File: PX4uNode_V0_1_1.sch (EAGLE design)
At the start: 133 parts, among them M3_MOUNT1101 MOUNT-HOLE3.1MM, M3_MOUNT1102 MOUNT-HOLE3.1MM, M3_MOUNT1103 MOUNT-HOLE3.1MM, M3_MOUNT1104 MOUNT-HOLE3.1MM, U101 STM32F4X7VX, U401 MAX3051, U402 MAX3051, X101 3.2x2.5 mm / 24 MHz / 15 ppm

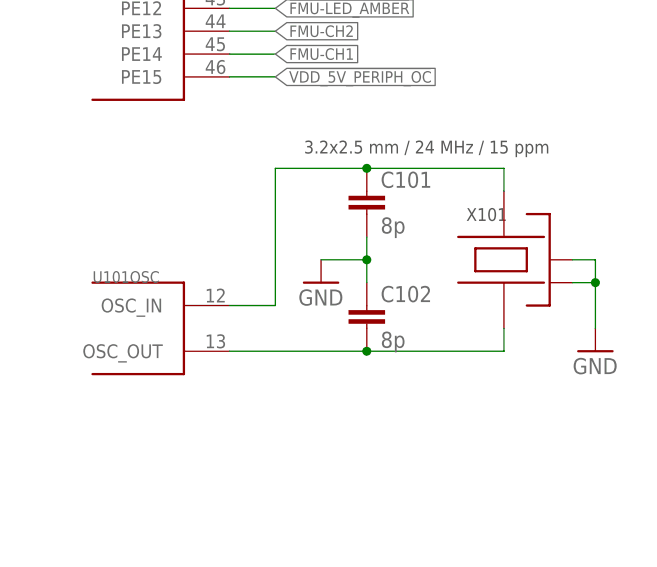
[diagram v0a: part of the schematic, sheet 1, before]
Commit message: A little more grounding
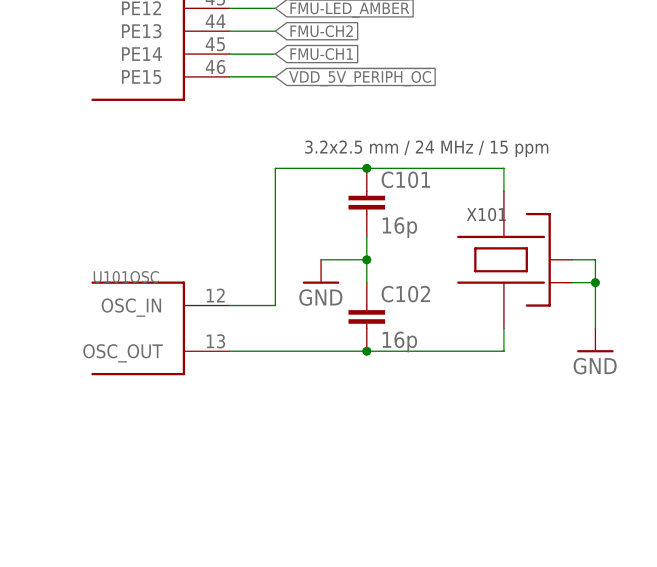
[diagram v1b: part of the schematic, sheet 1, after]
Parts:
- C101, C102: value 8p -> 16p; PARTNO C1005C0G1H080C -> C1005C0G1H160
- X101: PARTNO NX3225SA-24.000000MHZ -> ABM8G-24.000MHZ-4Y-T3
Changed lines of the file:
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@@
 <parts>
 <part name="X101" library="pixhawk2" deviceset="OSCILLATOR" device="-3.2X2.5" value="3.2x2.5 mm / 24 MHz / 15 ppm">
-<attribute name="PARTNO" value="NX3225SA-24.000000MHZ"/>
+<attribute name="PARTNO" value="ABM8G-24.000MHZ-4Y-T3"/>
 </part>
-<part name="C101" library="pixhawk2" deviceset="CAP" device="0402" value="8p">
-<attribute name="PARTNO" value="C1005C0G1H080C"/>
+<part name="C101" library="pixhawk2" deviceset="CAP" device="0402" value="16p">
+<attribute name="PARTNO" value="C1005C0G1H160"/>
 </part>
-<part name="C102" library="pixhawk2" deviceset="CAP" device="0402" value="8p">
-<attribute name="PARTNO" value="C1005C0G1H080C"/>
+<part name="C102" library="pixhawk2" deviceset="CAP" device="0402" value="16p">
+<attribute name="PARTNO" value="C1005C0G1H160"/>
 </part>
 <part name="GND1" library="SparkFun" deviceset="GND" device=""/>

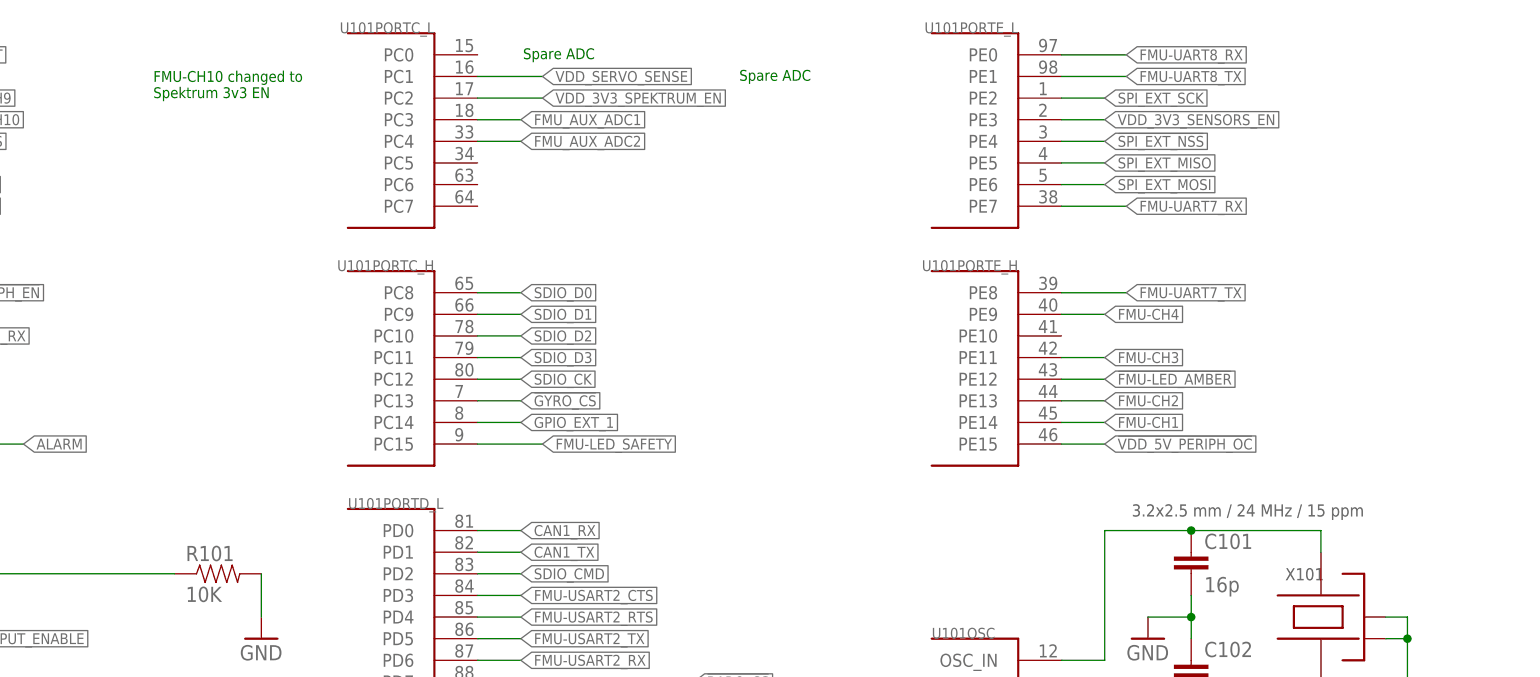
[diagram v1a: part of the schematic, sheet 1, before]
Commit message: General track thickening
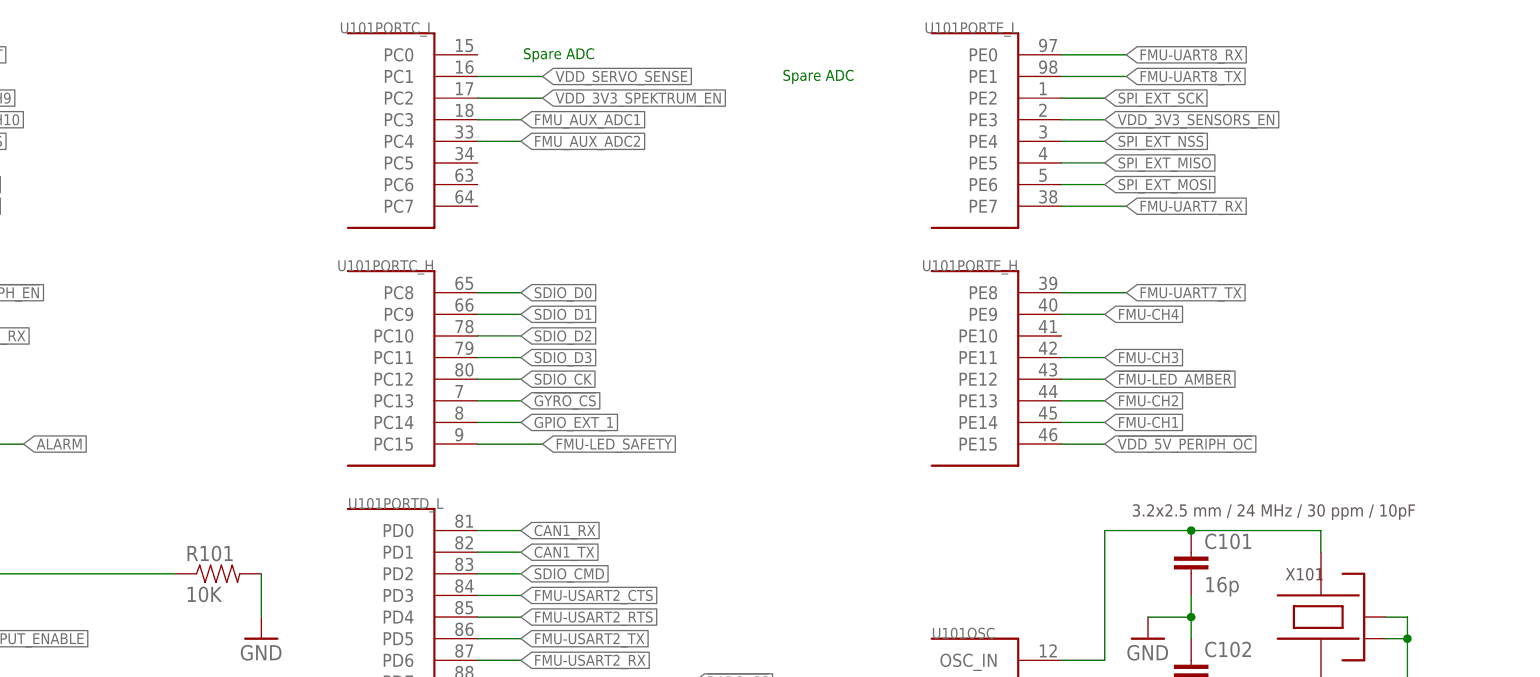
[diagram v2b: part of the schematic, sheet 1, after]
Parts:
- X101: value 3.2x2.5 mm / 24 MHz / 15 ppm -> 3.2x2.5 mm / 24 MHz / 30 ppm / 10pF
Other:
- note removed: "FMU-CH10 changed to Spektrum 3v3 EN"
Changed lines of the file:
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@@
 </classes>
 <parts>
-<part name="X101" library="pixhawk2" deviceset="OSCILLATOR" device="-3.2X2.5" value="3.2x2.5 mm / 24 MHz / 15 ppm">
+<part name="X101" library="pixhawk2" deviceset="OSCILLATOR" device="-3.2X2.5" value="3.2x2.5 mm / 24 MHz / 30 ppm / 10pF">
 <attribute name="PARTNO" value="ABM8G-24.000MHZ-4Y-T3"/>
 </part>
@@
 <text x="131.826" y="62.992" size="1.27" layer="91">Spare PWM output</text>
 <text x="112.014" y="164.592" size="1.27" layer="91">Spare ADC</text>
-<text x="137.414" y="162.052" size="1.27" layer="91">Spare ADC</text>
-<text x="68.58" y="160.02" size="1.27" layer="91">FMU-CH10 changed to
-Spektrum 3v3 EN</text>
+<text x="142.494" y="162.052" size="1.27" layer="91">Spare ADC</text>
 </plain>
 <instances>

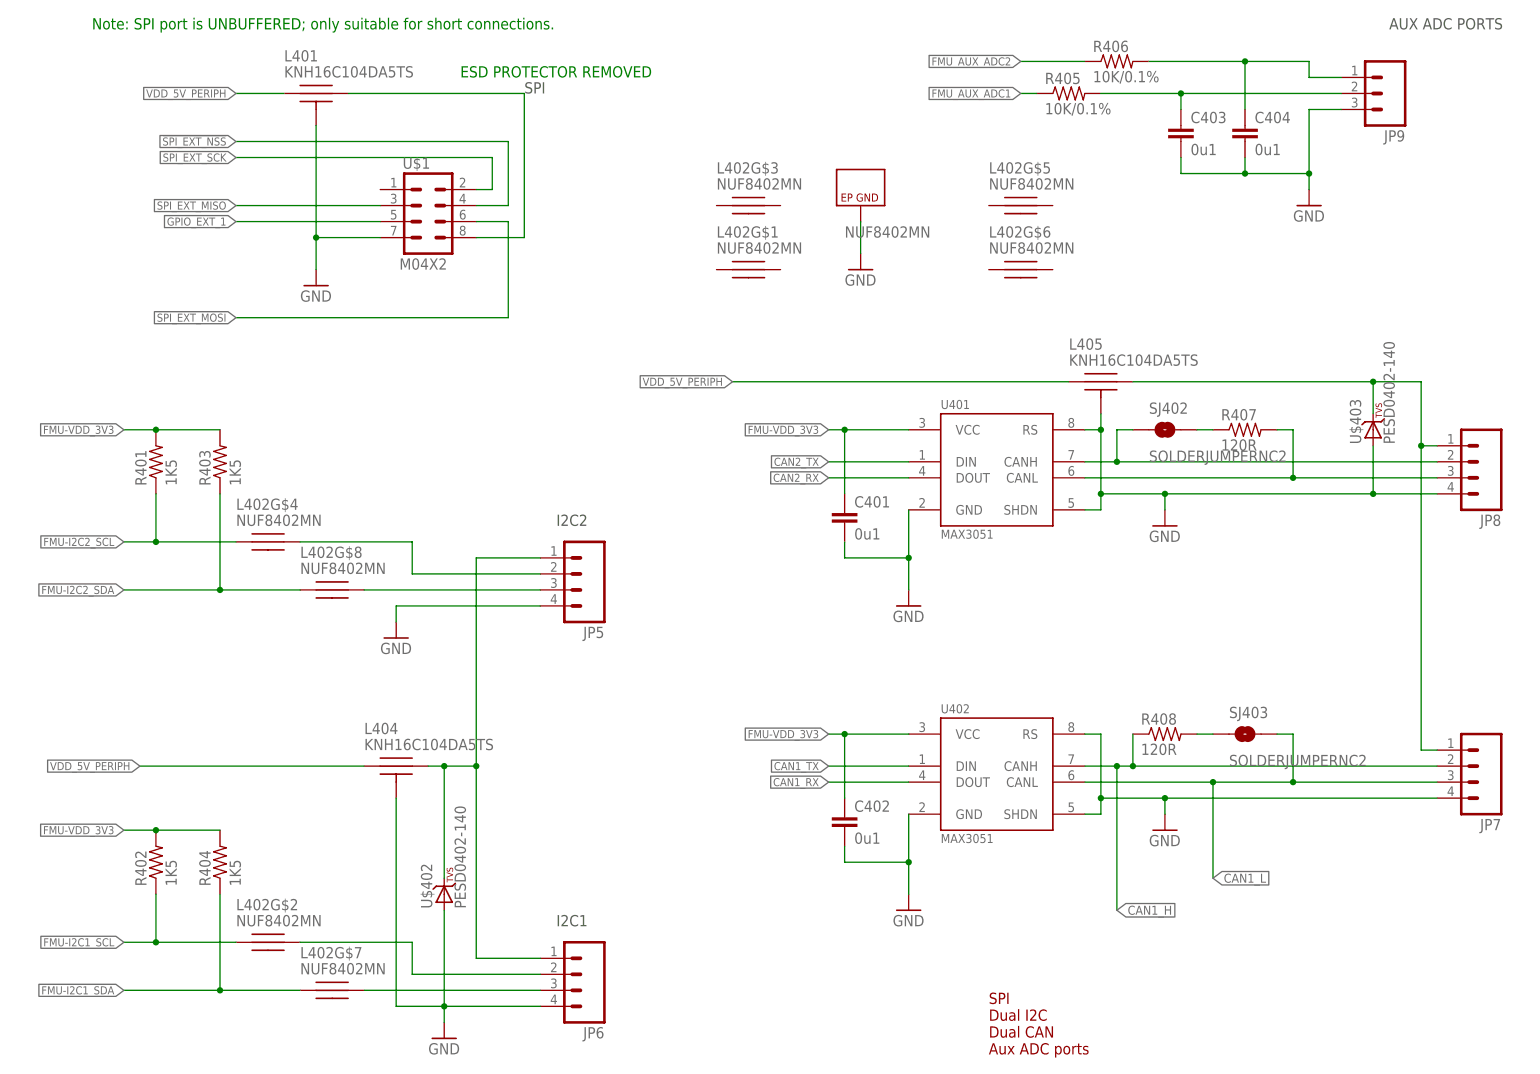
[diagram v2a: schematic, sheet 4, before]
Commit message: Added PARTNO and EXCLUDE to BOM. Parts renumbered
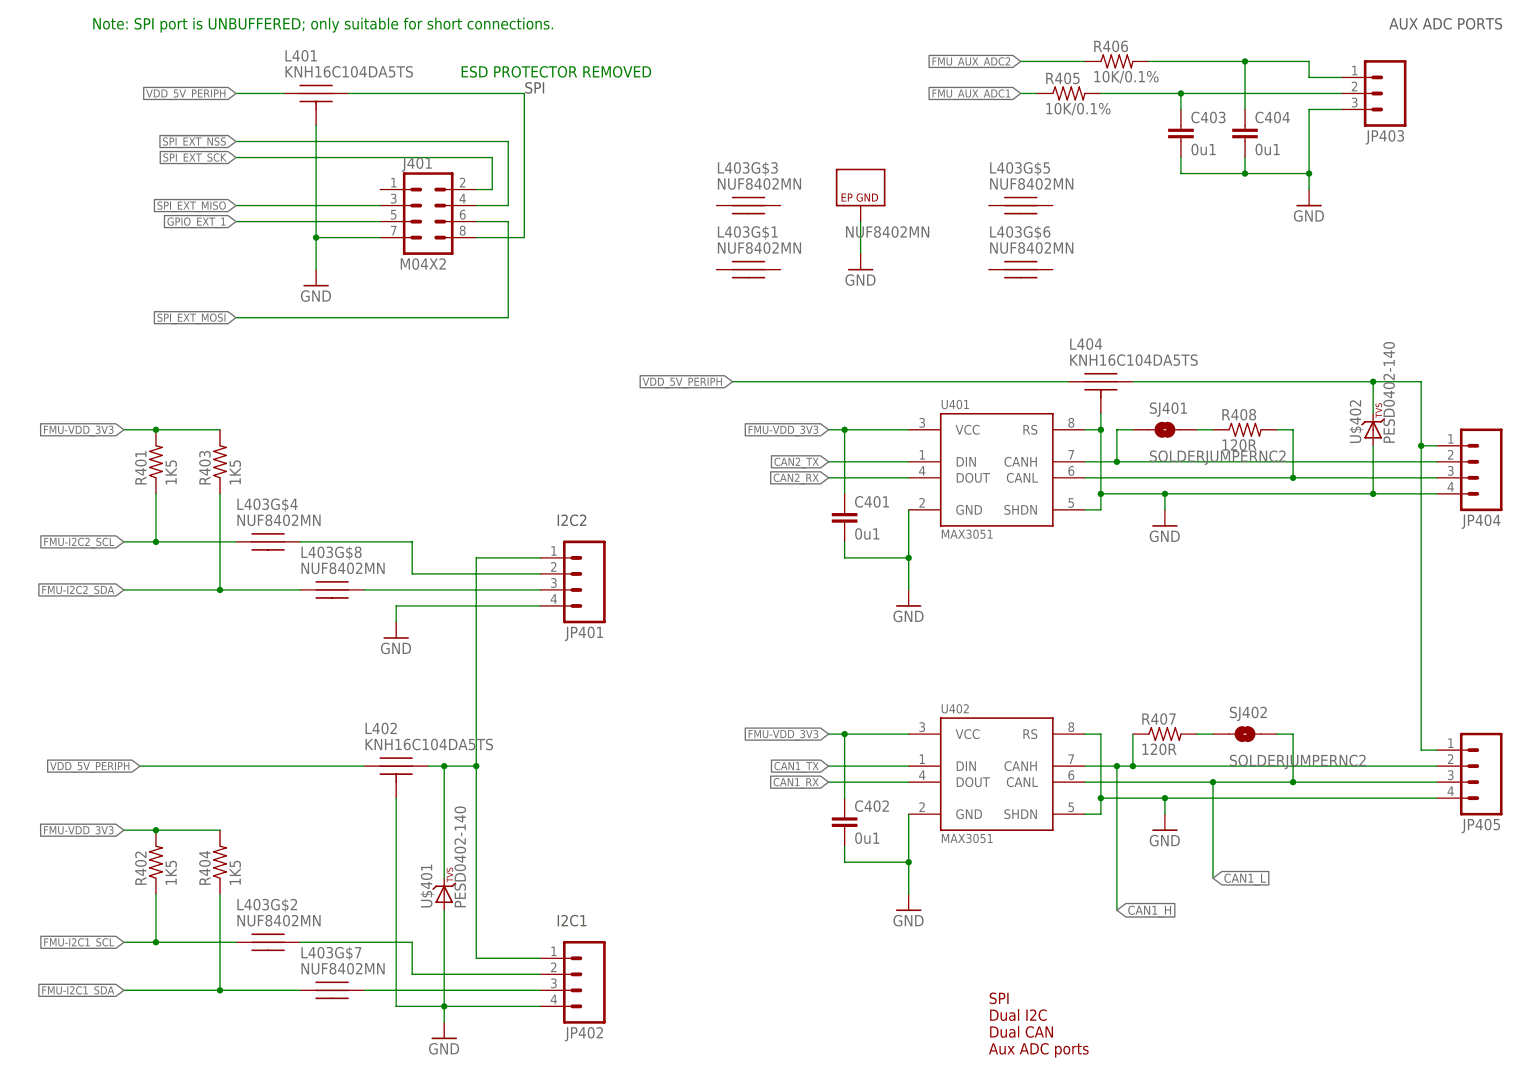
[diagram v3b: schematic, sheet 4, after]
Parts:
- removed C607: 22uF, SparkFun-Capacitors:22UF-16V-20%-(1210)
- removed C718: 2u2, pixhawk2:CAP0603
- removed L405: KNH16C104DA5TS, PX4lite:KNH16C104DA5TS
- removed R1: 10K, pixhawk2:RESISTOR0402-RES
- removed SJ403: SOLDERJUMPERNC2, SparkFun-Passives:SOLDERJUMPERNC2
- removed U$403, U$5: PESD0402-140, pixhawk2:DIODE-TVS
- added C604: 22uF, SparkFun-Capacitors:22UF-16V-20%-(1210)
- added C709: 0u1, pixhawk2:CAP0402
- added JP202: HEADER-3X1RA, PX4lite:HEADER-3X1RA
- added L403: NUF8402MN, PX4lite:NUF8402MN
- added R703: 47K, pixhawk2:RESISTOR0402-RES
- added SJ401: SOLDERJUMPERNC2, SparkFun-Passives:SOLDERJUMPERNC2
- added U$401: PESD0402-140, pixhawk2:DIODE-TVS
- C715, C717: value 0u1 -> 2u2; device pixhawk2:CAP0402 -> pixhawk2:CAP0603; PARTNO CC0402ZRY5V7BB104 -> C1608Y5V1C225Z
- C716: value 2u2 -> 0u1; device pixhawk2:CAP0603 -> pixhawk2:CAP0402; PARTNO C1608Y5V1C225Z -> CC0402ZRY5V7BB104
- D901, J401, JP203, JP204, JP205, JP301, JP401, JP402, JP404, JP405, JP801, U$704: BOM (none) -> EXCLUDE
- L402: value NUF8402MN -> KNH16C104DA5TS; device PX4lite:NUF8402MN -> PX4lite:KNH16C104DA5TS; PARTNO (none) -> KNH16C104DA5TS
- R704: value 47K -> 10K; PARTNO RMCF0402FT47K -> RC0402FR-0710KL
- U$201: value HEADER-3X1RA -> PESD0402-140; device PX4lite:HEADER-3X1RA -> pixhawk2:DIODE-TVS; PARTNO (none) -> PESD0402-140
- U$203: PARTNO (none) -> 74LVC2G240
- U$302: PARTNO (none) -> W25Q64FVZP
- U$501: PARTNO (none) -> MAX21100+
- renumbered D1 to D901, D2 to D701, JP1 to JP204, JP10 to JP801, JP11 to JP301, JP12 to JP203, JP13 to JP1101, JP2 to JP205, JP4 to JP1105, JP5 to JP401, JP6 to JP402, JP7 to JP405, JP8 to JP404, JP9 to JP403, L205 to L203, R2 to R203, R3 to R204, R4 to R201, R5 to R202, U$1 to J401, U$2 to U$203, U$205 to U$204, U$3 to U$202, U$4 to U$704
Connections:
- net !VDD_5V_PERIPH_EN: now also R704.2; no longer R705.2
- net !VDD_5V_PERIPH_OC: now also R705.2; no longer R1.2
- net CAN1_H: now also R407.1; no longer R408.1
- net CAN1_L: now also SJ402.2; no longer SJ403.2
- net CAN2_H: now also SJ401.1; no longer SJ402.1
- net CAN2_L: now also R408.2; no longer R407.2
- net FMU-!RESET: now also C713.2; no longer C714.2
- net FMU-I2C1_SCL: now also L403G$2.P$1; no longer L402G$2.P$1
- net FMU-I2C1_SDA: now also L403G$7.P$1; no longer L402G$7.P$1
- net FMU-I2C2_SCL: now also L403G$4.P$1; no longer L402G$4.P$1
- net FMU-I2C2_SDA: now also L403G$8.P$1; no longer L402G$8.P$1
- net FMU-VDD_3V3: now also C709.1, C714.1, C716.1, R704.1; no longer C713.1, C715.1, C717.1, R1.1
- net GND: now also C604.2, C709.2, C713.1, C714.2, JP202.3, L402.P$3, L403G$9.GND, R703.2, U$201.A, U$401.A; no longer C607.2, C713.2, C714.1, C718.2, L402G$9.GND, L405.P$3, R704.2, U$201.3, U$403.A, U$5.A
- net IC2_VDD_5V: now also L402.P$2, U$401.C; no longer L404.P$2, U$402.C
- net N$18: now also JP202.2, U$201.C; no longer U$201.2, U$5.C
- net N$2: now also JP202.1; no longer U$201.1
- net N$20: now also L403G$8.P$2; no longer L402G$8.P$2
- net N$21: now also R408.1, SJ401.2; no longer R407.1, SJ402.2
- net N$22: now also R407.2, SJ402.1; no longer R408.2, SJ403.1
- net N$28: now also L404.P$2, U$402.C; no longer L405.P$2, U$403.C
- net N$33: now also L403G$2.P$2; no longer L402G$2.P$2
- net N$34: now also R703.1; no longer R704.1
- net N$37: now also L403G$7.P$2; no longer L402G$7.P$2
- net N$4: now also L403G$4.P$2; no longer L402G$4.P$2
- net VCAP_1: now also C715.1; no longer C716.1
- net VCAP_2: now also C717.1; no longer C718.1
- net VDD_5V: now also C604.1; no longer C607.1
- net VDD_5V_PERIPH: now also L402.P$1; no longer L405.P$1
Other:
- moved on the sheet: C605, C606, C710, C711, C712, C713, C714, C715, C716, C717, L404, R407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

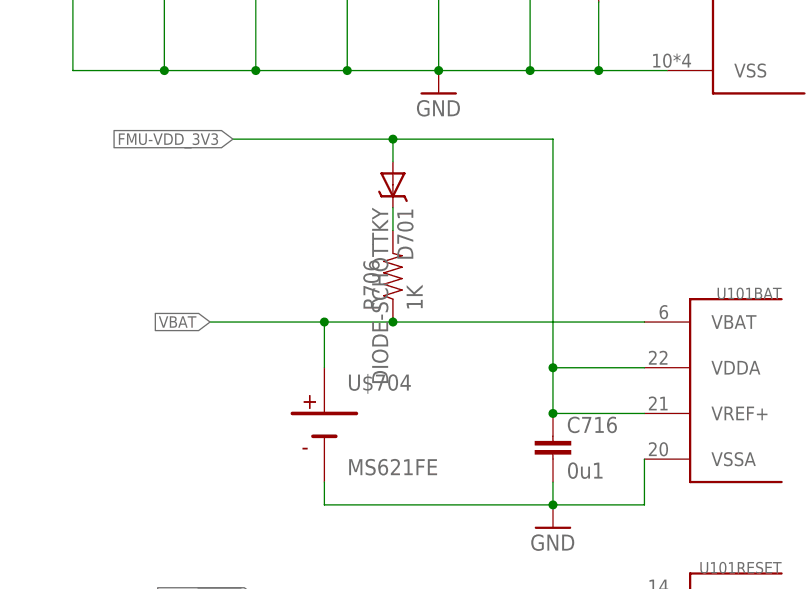
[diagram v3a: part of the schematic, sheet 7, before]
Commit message: More BOM tweaks
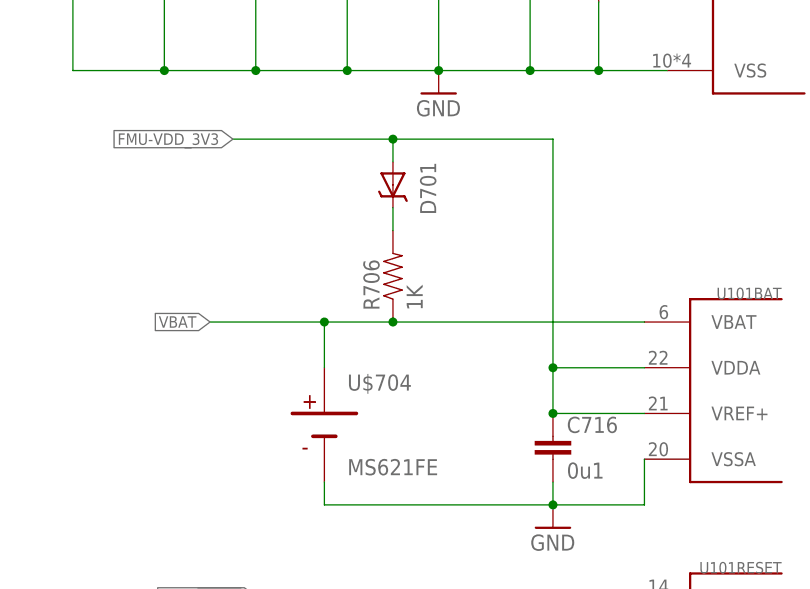
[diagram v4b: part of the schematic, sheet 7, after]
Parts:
- C601, C604, C605, C606: PARTNO (none) -> C3225X7R1C226M250AC
- D701: PARTNO (none) -> MBRA140
- D901: BOM EXCLUDE -> (none); PARTNO (none) -> MBRA140
- JP403: PARTNO (none) -> EXCLUDE
- L$601: PARTNO (none) -> XFL4020-222MEB
- L1001, L201, L202, L403: PARTNO (none) -> NUF8402MN
- U$301: PARTNO (none) -> NUF2042XV6
- U$601: PARTNO (none) -> TPS63061DSCT
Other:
- note removed: "DO NOT FIT"
